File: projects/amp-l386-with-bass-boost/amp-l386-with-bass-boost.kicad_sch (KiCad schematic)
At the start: 22 parts, among them U1 LM386

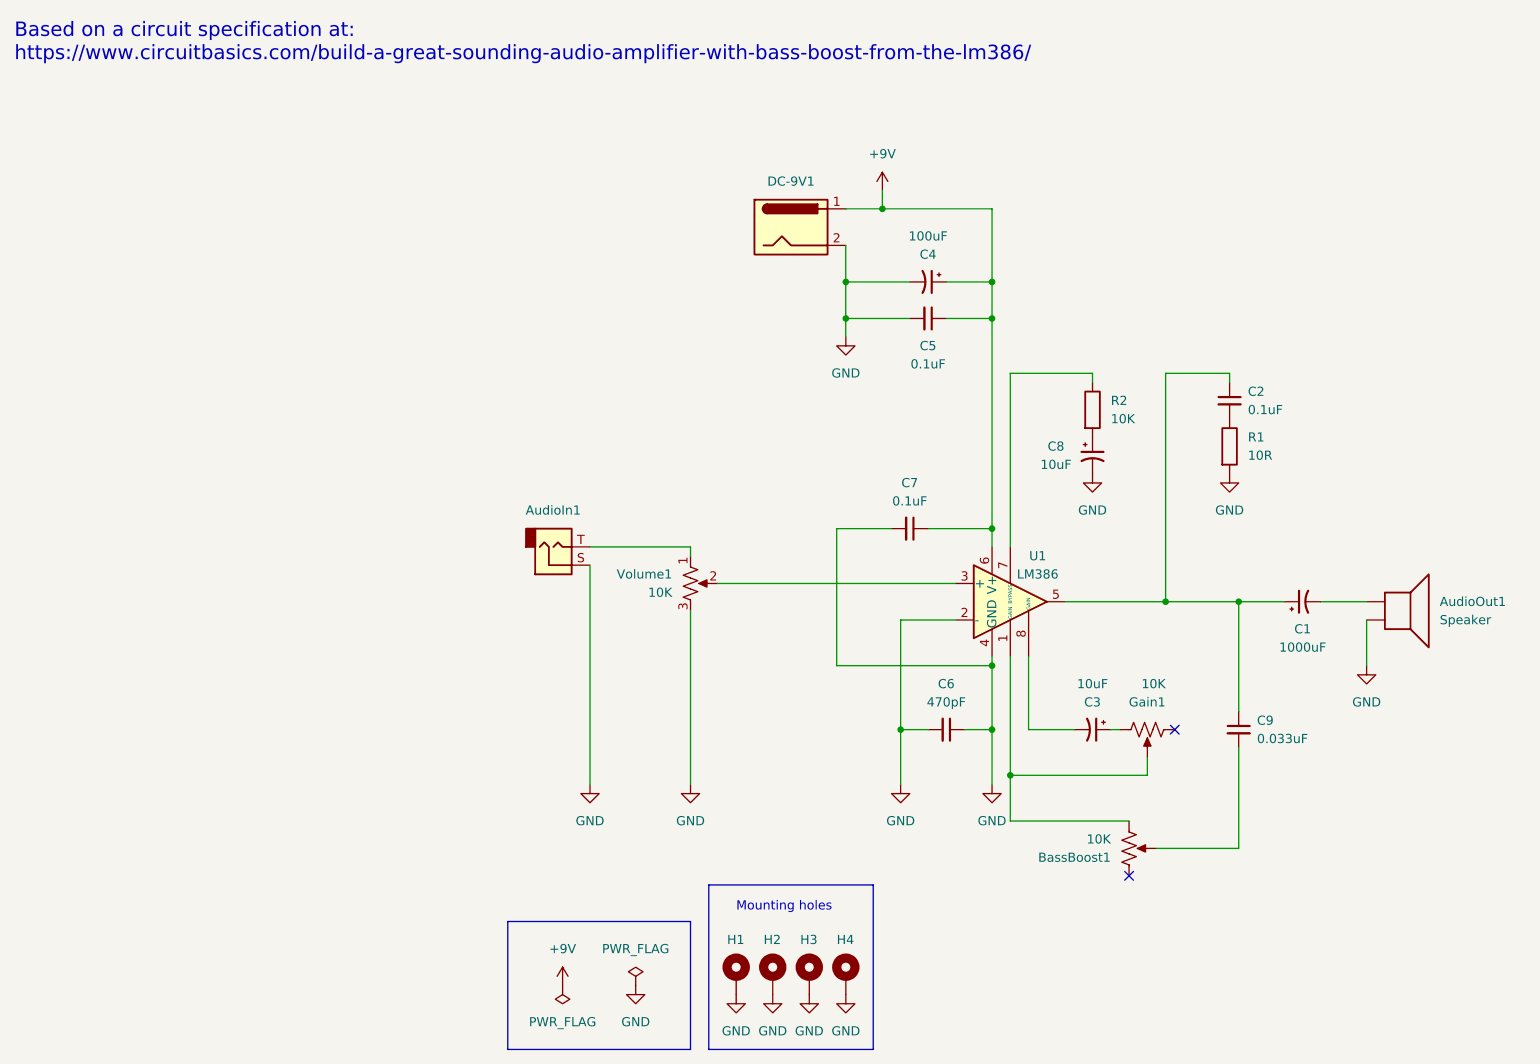
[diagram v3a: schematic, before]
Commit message: Add test points
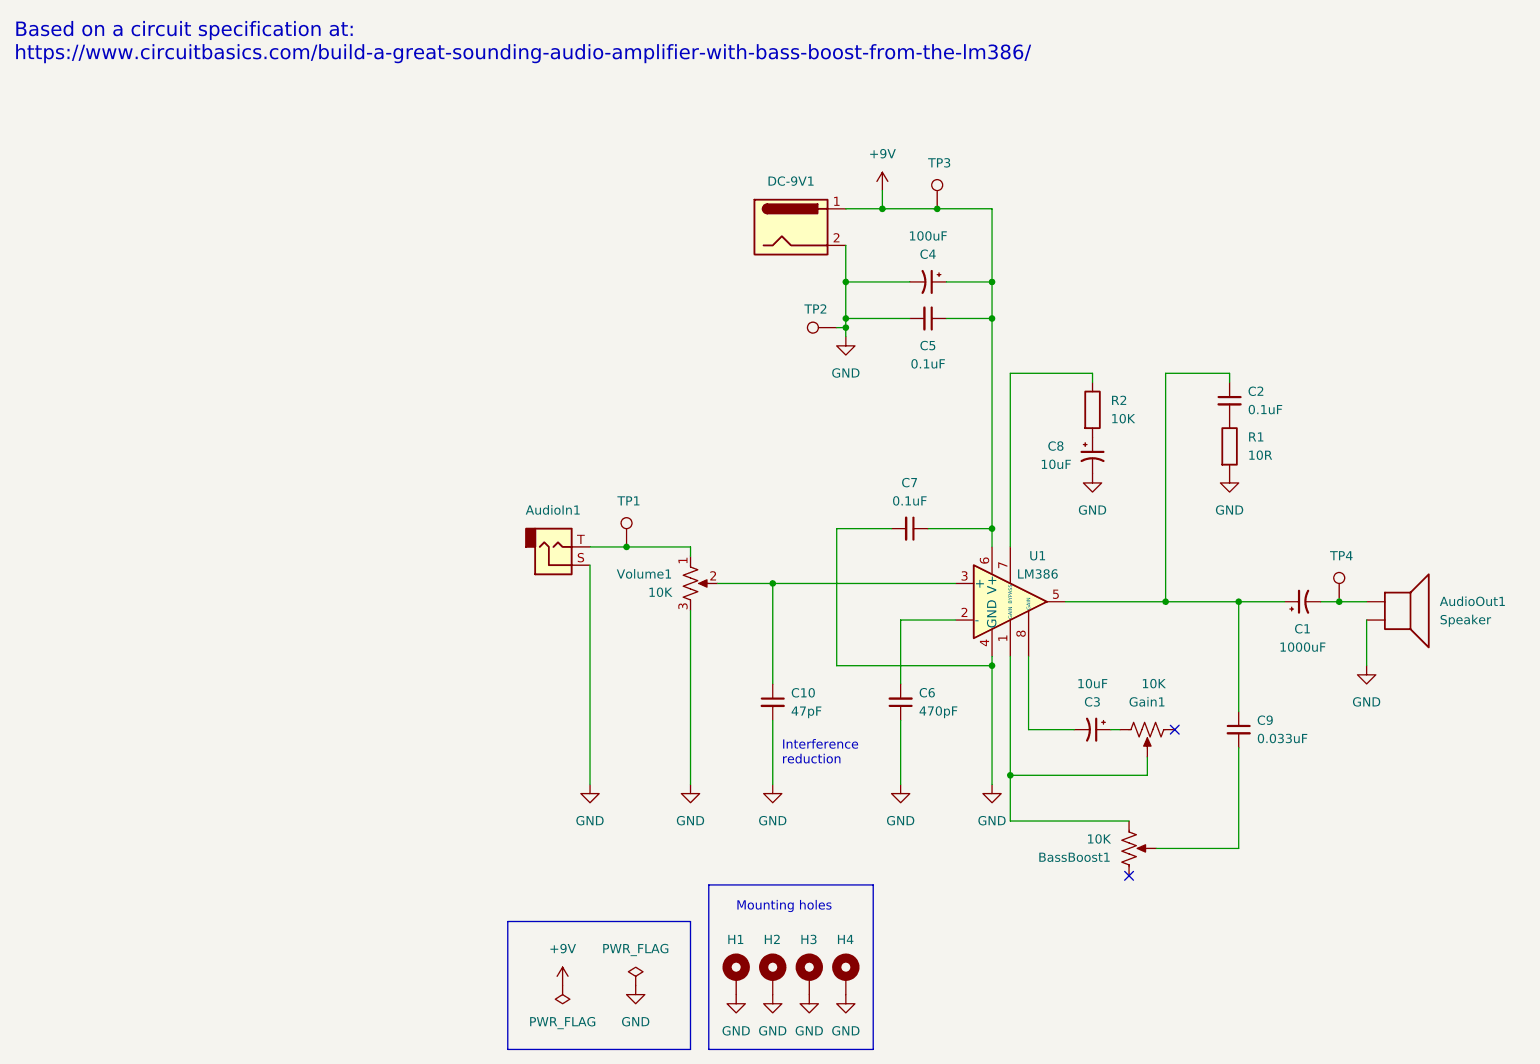
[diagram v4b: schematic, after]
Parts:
- added C10: 47pF, Capacitor_THT:C_Disc_D5.1mm_W3.2mm_P5.00mm, symbol Device:C_Small
- added TP1, TP2, TP3, TP4: TestPoint, TestPoint:TestPoint_Pad_2.0x2.0mm, symbol Connector:TestPoint
- C1: footprint Capacitor_THT:CP_Axial_L10.0mm_D4.5mm_P15.00mm_Horizontal -> Capacitor_THT:CP_Radial_D10.0mm_P5.00mm; Notes (none) -> electrolytic
- C2, C7, C9: footprint Capacitor_THT:CP_Axial_L10.0mm_D4.5mm_P15.00mm_Horizontal -> Capacitor_THT:C_Disc_D5.1mm_W3.2mm_P5.00mm; Notes (none) -> ceramic
- C3, C8: footprint Capacitor_THT:CP_Axial_L10.0mm_D4.5mm_P15.00mm_Horizontal -> Capacitor_THT:CP_Radial_D5.0mm_P2.50mm; Notes (none) -> electrolytic
- C4: footprint Capacitor_THT:CP_Axial_L10.0mm_D4.5mm_P15.00mm_Horizontal -> Capacitor_THT:CP_Radial_D6.3mm_P2.50mm; Notes (none) -> electrolytic
- C5: footprint Capacitor_THT:CP_Axial_L10.0mm_D4.5mm_P15.00mm_Horizontal -> Capacitor_THT:C_Rect_L7.0mm_W2.5mm_P5.00mm; Notes (none) -> film
- C6: footprint Capacitor_THT:CP_Axial_L10.0mm_D4.5mm_P15.00mm_Horizontal -> Capacitor_THT:C_Rect_L7.0mm_W2.5mm_P5.00mm; Notes (none) -> Mylar polyester film
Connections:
- net +9V: now also TP3.1
- net GND: now also C10.2, TP2.1; no longer C6.2, U1.2 (-)
- net at AudioIn1.T, Volume1.1: now also TP1.1
- net at U1.3 (+), Volume1.2: now also C10.1
- net at AudioOut1.1, C1.2: now also TP4.1
- new net: C6.2, U1.2 (-)
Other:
- note added: "Interference reduction"
- moved on the sheet: C6
